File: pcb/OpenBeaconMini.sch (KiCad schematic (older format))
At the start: 79 parts, among them J1 Bias V, J10 UART, J11 BNC, J2 PAI+, J3 PAI-, J4 Digital IO, J5 ADC Inputs, J6 SMA, J7 SMA, J8 I2C Bus, J9 GND, K1 G5V-1-DC5, K2 G5V-1-DC5, M1 LPF 1, M2 LPF 2, Q1 2N7002, Q2 MMBT4403, Q3 2SK3074, Q4 2N7002, Q5 2N7002, Q6 2N7002, U1 TLV61046A, U2 ASTX-H11-25.000MHZ-T, U3 SN74LVC1G17, U4 SI5351A, U5 MCP4725A1T-E/CH, U6 128x32 OLED, U7 Empyrean, U8 24AA64T

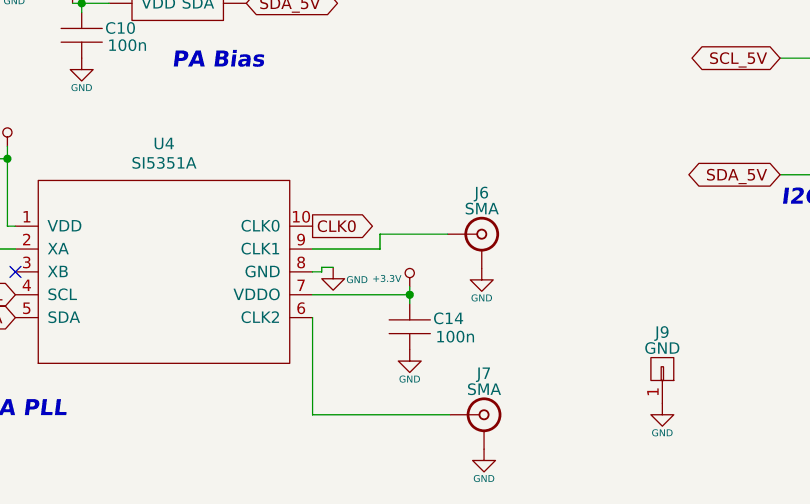
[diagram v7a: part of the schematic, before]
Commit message: Initial sl support for FT8
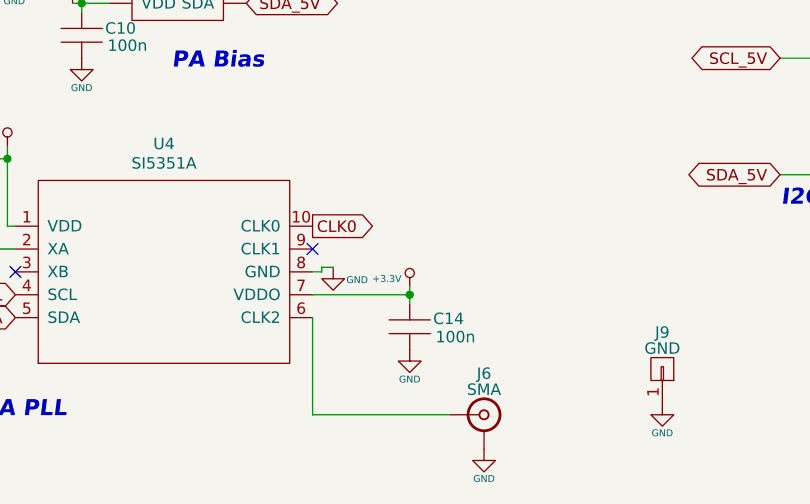
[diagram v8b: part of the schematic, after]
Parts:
- removed J6: SMA, EtherkitKicadLibrary:SMA-ENDLAUNCH, symbol EtherkitKicadLibrary:BNC
- J10, J4, J8: footprint Pin_Headers:Pin_Header_Straight_1x04_Pitch2.54mm -> Connector_PinHeader_2.54mm:PinHeader_1x04_P2.54mm_Vertical
- J5: footprint Pin_Headers:Pin_Header_Straight_1x06_Pitch2.54mm -> Connector_PinHeader_2.54mm:PinHeader_1x06_P2.54mm_Vertical
- renumbered J7 to J6
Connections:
- no-connect marks 9 -> 10
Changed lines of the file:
@@
 A4
 $Comp
-L EtherkitKicadLibrary:BNC J7
+L EtherkitKicadLibrary:BNC J6
 U 1 1 5A24B150
 P 5050 7595
-F 0 "J7" H 5050 7775 50  0000 C CNN
+F 0 "J6" H 5050 7775 50  0000 C CNN
 F 1 "SMA" H 5050 7705 50  0000 C CNN
 F 2 "EtherkitKicadLibrary:SMA-ENDLAUNCH" H 5050 7595 60  0001 C CNN
@@
 F 0 "J5" H 4680 1300 50  0000 C CNN
 F 1 "ADC Inputs" H 4680 585 50  0000 C CNN
-F 2 "Pin_Headers:Pin_Header_Straight_1x06_Pitch2.54mm" H 4680 995 50  0001 C CNN
+F 2 "Connector_PinHeader_2.54mm:PinHeader_1x06_P2.54mm_Vertical" H 4680 995 50  0001 C CNN
 F 3 "" H 4680 995 50  0001 C CNN
 	1    4680 995
@@
 F 0 "J8" H 5430 1195 50  0000 C CNN
 F 1 "I2C Bus" H 5430 695 50  0000 C CNN
-F 2 "Pin_Headers:Pin_Header_Straight_1x04_Pitch2.54mm" H 5430 995 50  0001 C CNN
+F 2 "Connector_PinHeader_2.54mm:PinHeader_1x04_P2.54mm_Vertical" H 5430 995 50  0001 C CNN
 F 3 "" H 5430 995 50  0001 C CNN
 	1    5430 995
@@
 Text GLabel 5230 1095 0    50   BiDi ~ 0
 SDA
-$Comp
-L EtherkitKicadLibrary:BNC J6
-U 1 1 5A251F5A
-P 5040 6805
-F 0 "J6" H 5040 6985 50  0000 C CNN
-F 1 "SMA" H 5040 6915 50  0000 C CNN
-F 2 "EtherkitKicadLibrary:SMA-ENDLAUNCH" H 5040 6805 60  0001 C CNN
-F 3 "" H 5040 6805 60  0000 C CNN
-	1    5040 6805
-	1    0    0    -1
-$EndComp
-$Comp
-L OpenBeaconMini-rescue:GND #PWR034
-U 1 1 5A25206E
-P 5040 6955
-F 0 "#PWR034" H 5040 6705 50  0001 C CNN
-F 1 "GND" H 5040 6825 30  0000 C CNN
-F 2 "" H 5040 6955 50  0001 C CNN
-F 3 "" H 5040 6955 50  0001 C CNN
-	1    5040 6955
-	1    0    0    -1
-$EndComp
-Wire Wire Line
-	4890 6805 4595 6805
-Wire Wire Line
-	4595 6805 4595 6870
-Wire Wire Line
-	4595 6870 4300 6870
 $Comp
 L EtherkitKicadLibrary:+5V #PWR019
@@
 F 0 "J4" H 3875 1195 50  0000 C CNN
 F 1 "Digital IO" H 3875 695 50  0000 C CNN
-F 2 "Pin_Headers:Pin_Header_Straight_1x04_Pitch2.54mm" H 3875 995 50  0001 C CNN
+F 2 "Connector_PinHeader_2.54mm:PinHeader_1x04_P2.54mm_Vertical" H 3875 995 50  0001 C CNN
 F 3 "" H 3875 995 50  0001 C CNN
 	1    3875 995
@@
 F 0 "J10" H 6155 1195 50  0000 C CNN
 F 1 "UART" H 6155 695 50  0000 C CNN
-F 2 "Pin_Headers:Pin_Header_Straight_1x04_Pitch2.54mm" H 6155 995 50  0001 C CNN
+F 2 "Connector_PinHeader_2.54mm:PinHeader_1x04_P2.54mm_Vertical" H 6155 995 50  0001 C CNN
 F 3 "" H 6155 995 50  0001 C CNN
 	1    6155 995
@@
 	7280 2775 7280 2760
 Connection ~ 7280 2760
+NoConn ~ 4300 6870
 $EndSCHEMATC
